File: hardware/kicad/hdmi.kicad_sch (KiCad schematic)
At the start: 1 part, among them J1 HDMI_C_1.4

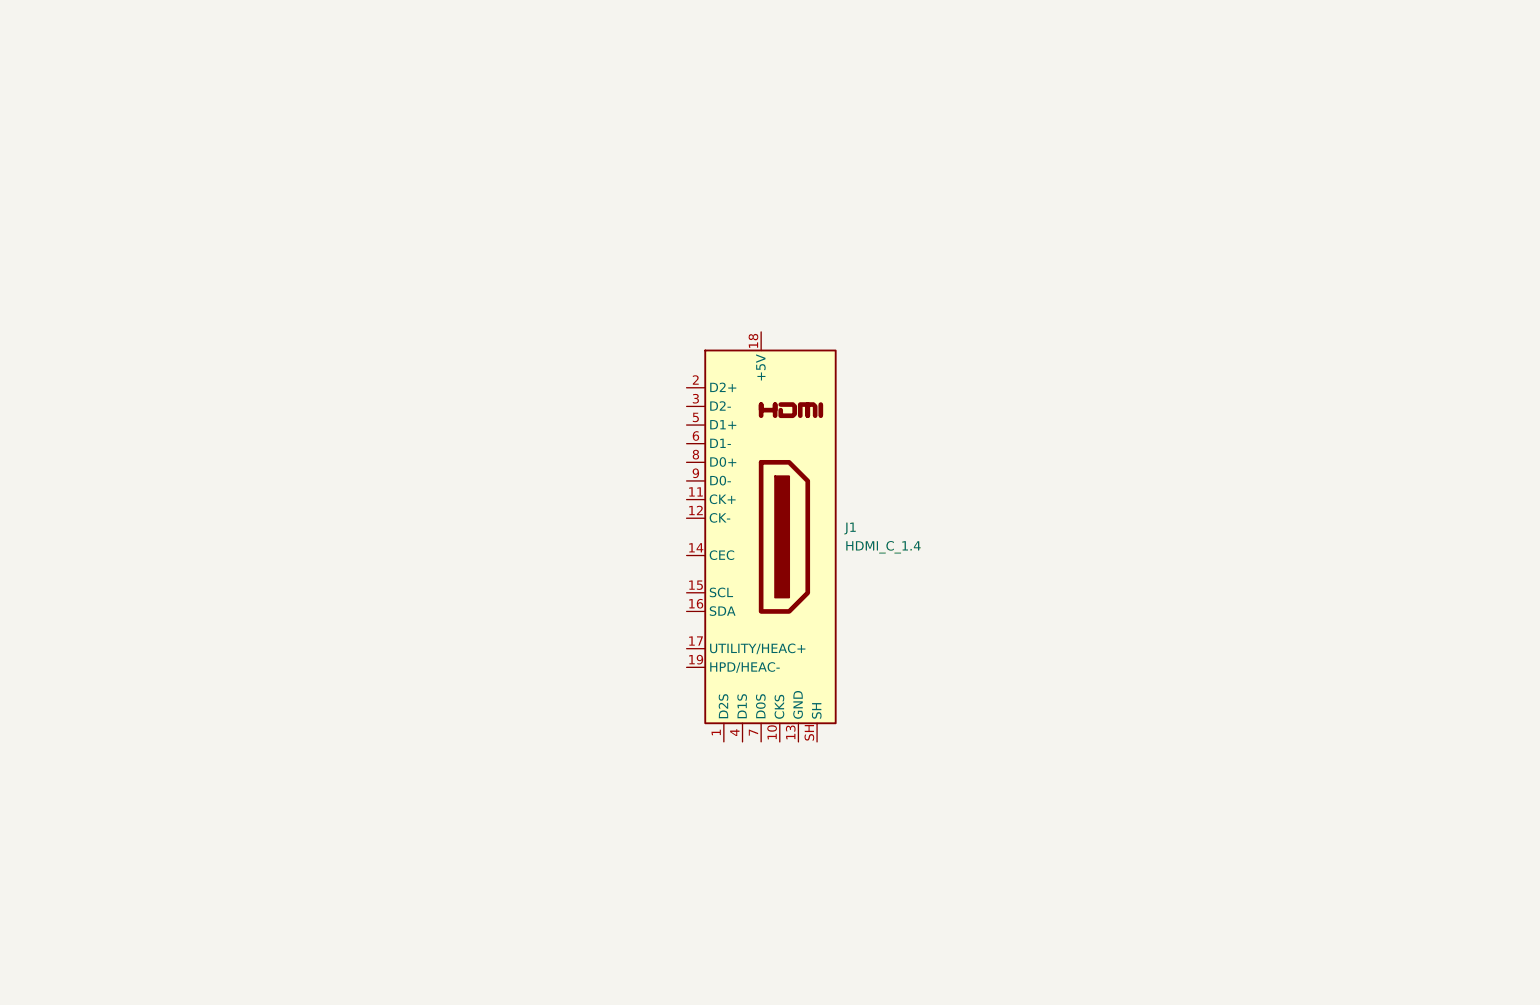
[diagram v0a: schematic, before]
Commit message: layout: finish dq0 & dq1 routing
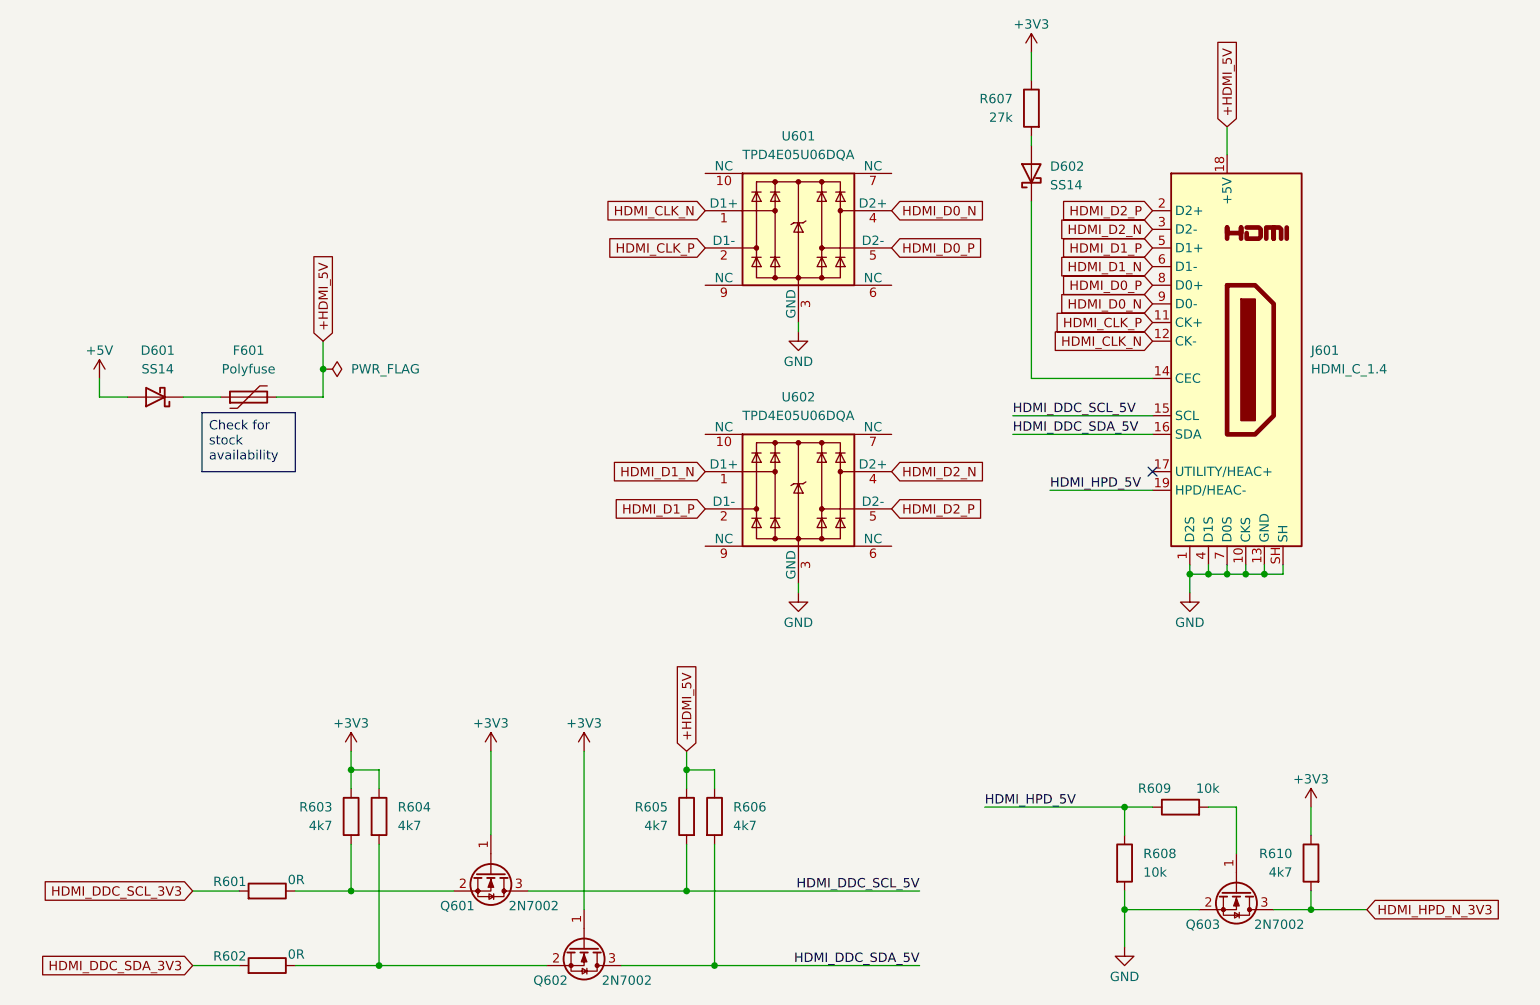
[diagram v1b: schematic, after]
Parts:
- added D601, D602: SS14, Diode_SMD:D_SMA, symbol Diode:SS14
- added F601: Polyfuse, Fuse:Fuse_0603_1608Metric, symbol Device:Polyfuse
- added Q601, Q602, Q603: 2N7002, Package_TO_SOT_SMD:SOT-23, symbol Transistor_FET:2N7002
- added R601, R602: 0R, Resistor_SMD:R_0402_1005Metric, symbol Device:R
- added R603, R604, R605, R606, R610: 4k7, Resistor_SMD:R_0402_1005Metric, symbol Device:R
- added R607: 27k, Resistor_SMD:R_0603_1608Metric, symbol Device:R
- added R608, R609: 10k, Resistor_SMD:R_0402_1005Metric, symbol Device:R
- added U601, U602: TPD4E05U06DQA, Package_SON:USON-10_2.5x1.0mm_P0.5mm, symbol Power_Protection:TPD4E05U06DQA
- renumbered J1 to J601
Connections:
- net GND: now reaches J601.1 (D2S)
- net GND: now also J601.10 (CKS), J601.13 (GND), J601.4 (D1S), J601.7 (D0S), J601.SH, Q603.2 (S), R608.2, U601.3 (GND), U601.8 (GND), U602.3 (GND), U602.8 (GND)
- net HDMI_CLK_P: now reaches J601.11 (CK+)
- net HDMI_CLK_P: now also U601.2 (D1-)
- net HDMI_CLK_N: now reaches J601.12 (CK-)
- net HDMI_CLK_N: now also U601.1 (D1+)
- net at J601.14 (CEC): now also D602.1 (K)
- net HDMI_DDC_SCL_5V: now reaches J601.15 (SCL)
- net HDMI_DDC_SCL_5V: now also Q601.3 (D), R605.2
- net HDMI_DDC_SDA_5V: now reaches J601.16 (SDA)
- net HDMI_DDC_SDA_5V: now also Q602.3 (D), R606.2
- net +HDMI_5V: now reaches J601.18 (+5V)
- net +HDMI_5V: now also F601.2, R605.1, R606.1
- net HDMI_HPD_5V: now reaches J601.19 (HPD/HEAC-)
- net HDMI_HPD_5V: now also R608.1, R609.1
- net HDMI_D2_P: now reaches J601.2 (D2+)
- net HDMI_D2_P: now also U602.5 (D2-)
- net HDMI_D2_N: now reaches J601.3 (D2-)
- net HDMI_D2_N: now also U602.4 (D2+)
- net HDMI_D1_P: now reaches J601.5 (D1+)
- net HDMI_D1_P: now also U602.2 (D1-)
- net HDMI_D1_N: now reaches J601.6 (D1-)
- net HDMI_D1_N: now also U602.1 (D1+)
- net HDMI_D0_P: now reaches J601.8 (D0+)
- net HDMI_D0_P: now also U601.5 (D2-)
- net HDMI_D0_N: now reaches J601.9 (D0-)
- net HDMI_D0_N: now also U601.4 (D2+)
- new net: Q603.1 (G), R609.2
- new net: D601.1 (K), F601.1
- new net: Q602.2 (S), R602.1, R604.2
- new net: D602.2 (A), R607.2
- new net: Q601.2 (S), R601.1, R603.2
- new net +3V3: Q601.1 (G), Q602.1 (G), R603.1, R604.1, R607.1, R610.1
- new net +5V: D601.2 (A)
- new net HDMI_DDC_SCL_3V3: R601.2
- new net HDMI_DDC_SDA_3V3: R602.2
- new net HDMI_HPD_N_3V3: Q603.3 (D), R610.2
- no-connect marks 0 -> 1
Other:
- moved on the sheet: J601

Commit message: finish basic ddr routing
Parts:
- removed J601: HDMI_C_1.4, Projects:HDMI-SMD_A71-05H4-111N1, symbol Connector:HDMI_C_1.4
- added J602: HDMI_A_1.4, Connector_Video:HDMI_A_Amphenol_10029449-x01xLF_Horizontal, symbol Connector:HDMI_A_1.4
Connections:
- net +HDMI_5V: now also J602.18 (+5V)
- net GND: now also J602.11 (CKS), J602.17 (GND), J602.2 (D2S), J602.5 (D1S), J602.8 (D0S), J602.SH
- net HDMI_CLK_N: now also J602.12 (CK-)
- net HDMI_CLK_P: now also J602.10 (CK+)
- net HDMI_D0_N: now also J602.9 (D0-)
- net HDMI_D0_P: now also J602.7 (D0+)
- net HDMI_D1_N: now also J602.6 (D1-)
- net HDMI_D1_P: now also J602.4 (D1+)
- net HDMI_D2_N: now also J602.3 (D2-)
- net HDMI_D2_P: now also J602.1 (D2+)
- net HDMI_DDC_SCL_5V: now also J602.15 (SCL)
- net HDMI_DDC_SDA_5V: now also J602.16 (SDA)
- net HDMI_HPD_5V: now also J602.19 (HPD/HEAC-)
- net at D602.1 (K): now also J602.13 (CEC)
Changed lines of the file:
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@@
+	)
+	(symbol
+		(lib_id "Connector:HDMI_A_1.4")
+		(at 207.01 63.5 0)
+		(unit 1)
+		(body_style 1)
+		(exclude_from_sim no)
+		(in_bom yes)
+		(on_board yes)
+		(in_pos_files yes)
+		(dnp no)
+		(fields_autoplaced yes)
+		(property "Reference" "J602"
+			(at 218.44 62.2299 0)
+			(show_name no)
+			(do_not_autoplace no)
+			(effects
+				(font
+					(size 1.27 1.27)
+				)
+				(justify left)
+			)
+		)
+		(property "Value" "HDMI_A_1.4"
+			(at 218.44 64.7699 0)
+			(show_name no)
+			(do_not_autoplace no)
+			(effects
+				(font
+					(size 1.27 1.27)
+				)
+				(justify left)
+			)
+		)
+		(property "Footprint" "Connector_Video:HDMI_A_Amphenol_10029449-x01xLF_Horizontal"
+			(at 207.645 63.5 0)
+			(hide yes)
+			(show_name no)
+			(do_not_autoplace no)
+			(effects
+				(font
+					(size 1.27 1.27)
+				)
+			)
+		)
+		(property "Datasheet" "https://en.wikipedia.org/wiki/HDMI"
+			(at 207.645 63.5 0)
+			(hide yes)
+			(show_name no)
+			(do_not_autoplace no)
+			(effects
+				(font
+					(size 1.27 1.27)
+				)
+			)
+		)
+		(property "Description" "HDMI 1.4+ type A connector"
+			(at 207.01 63.5 0)
+			(hide yes)
+			(show_name no)
+			(do_not_autoplace no)
+			(effects
+				(font
+					(size 1.27 1.27)
+				)
+			)
+		)
+		(pin "6"
+		)
+		(pin "5"
+		)
+		(pin "4"
+		)
+		(pin "3"
+		)
+		(pin "2"
+		)
+		(pin "1"
+		)
+		(pin "7"
+		)
+		(pin "19"
+		)
+		(pin "SH"
+		)
+		(pin "8"
+		)
+		(pin "9"
+		)
+		(pin "10"
+		)
+		(pin "11"
+		)
+		(pin "12"
+		)
+		(pin "13"
+		)
+		(pin "14"
+		)
+		(pin "15"
+		)
+		(pin "16"
+		)
+		(pin "17"
+		)
+		(pin "18"
+		)
+		(instances
+			(project "ZYNQ_PI_Zero"
+				(path "/e0cc3273-981b-466d-ad17-67861c989a34/194bd49b-39b9-439e-9b76-18223c8ed8de"
+					(reference "J602")
+					(unit 1)
+				)
+			)
+		)
 	)
 	(symbol
@@
 	)
 	(symbol
-		(lib_id "Connector:HDMI_C_1.4")
-		(at 207.01 63.5 0)
-		(unit 1)
-		(body_style 1)
-		(exclude_from_sim no)
-		(in_bom yes)
-		(on_board yes)
-		(in_pos_files yes)
-		(dnp no)
-		(fields_autoplaced yes)
-		(property "Reference" "J601"
-			(at 218.44 62.2299 0)
-			(show_name no)
-			(do_not_autoplace no)
-			(effects
-				(font
-					(size 1.27 1.27)
-				)
-				(justify left)
-			)
-		)
-		(property "Value" "HDMI_C_1.4"
-			(at 218.44 64.7699 0)
-			(show_name no)
-			(do_not_autoplace no)
-			(effects
-				(font
-					(size 1.27 1.27)
-				)
-				(justify left)
-			)
-		)
-		(property "Footprint" "Projects:HDMI-SMD_A71-05H4-111N1"
-			(at 207.645 63.5 0)
-			(hide yes)
-			(show_name no)
-			(do_not_autoplace no)
-			(effects
-				(font
-					(size 1.27 1.27)
-				)
-			)
-		)
-		(property "Datasheet" "http://pinoutguide.com/PortableDevices/mini_hdmi_pinout.shtml"
-			(at 207.645 63.5 0)
-			(hide yes)
-			(show_name no)
-			(do_not_autoplace no)
-			(effects
-				(font
-					(size 1.27 1.27)
-				)
-			)
-		)
-		(property "Description" "HDMI 1.4+ type C connector"
-			(at 207.01 63.5 0)
-			(hide yes)
-			(show_name no)
-			(do_not_autoplace no)
-			(effects
-				(font
-					(size 1.27 1.27)
-				)
-			)
-		)
-		(pin "6"
-		)
-		(pin "5"
-		)
-		(pin "1"
-		)
-		(pin "2"
-		)
-		(pin "3"
-		)
-		(pin "4"
-		)
-		(pin "11"
-		)
-		(pin "14"
-		)
-		(pin "10"
-		)
-		(pin "7"
-		)
-		(pin "SH"
-		)
-		(pin "18"
-		)
-		(pin "17"
-		)
-		(pin "19"
-		)
-		(pin "15"
-		)
-		(pin "16"
-		)
-		(pin "8"
-		)
-		(pin "12"
-		)
-		(pin "9"
-		)
-		(pin "13"
-		)
-		(instances
-			(project "hdmi"
-				(path "/73962548-2d49-4c88-a3cb-78a30267d693"
-					(reference "J1")
-					(unit 1)
-				)
-			)
-			(project "ZYNQ_PI_Zero"
-				(path "/e0cc3273-981b-466d-ad17-67861c989a34/194bd49b-39b9-439e-9b76-18223c8ed8de"
-					(reference "J601")
-					(unit 1)
-				)
-			)
-		)
-	)
-	(symbol
 		(lib_id "Power_Protection:TPD4E05U06DQA")
 		(at 148.59 45.72 0)
@@
 		)
 	)
+	(group ""
+		(members "15ec8058-eab1-47b0-89ef-e2197ceaa15e" "393eb2c9-2556-4fee-b569-2b447a7b0a4b"
+			"53660a61-2632-4e15-adf6-5c5c47ac1d81" "a32247c4-e007-4166-9461-d745543ec6ca"
+			"c5efe4c3-ab68-4d84-91f1-3170fa4f51b5" "c7352788-c409-47d4-88d6-23826d82852c"
+			"c9fb8644-763e-4d68-aa22-a40db3cfe74b" "cbd01b89-5dcc-49a2-98e9-251aa4bc034f"
+		)
+	)

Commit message: feat: need switch two singals of SD inferface
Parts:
- F601: footprint Fuse:Fuse_0603_1608Metric -> Fuse:Fuse_0805_2012Metric
- J602: footprint Connector_Video:HDMI_A_Amphenol_10029449-x01xLF_Horizontal -> Project:HDMI-SMD_HDMI-19PIN-043_C2858275
- R608, R609: footprint Resistor_SMD:R_0402_1005Metric -> Resistor_SMD:R_0603_1608Metric
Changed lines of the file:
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@@
 			)
 		)
-		(property "Footprint" "Resistor_SMD:R_0402_1005Metric"
+		(property "Footprint" "Resistor_SMD:R_0603_1608Metric"
 			(at 200.66 126.238 90)
 			(hide yes)
@@
 			)
 		)
-		(property "Footprint" "Connector_Video:HDMI_A_Amphenol_10029449-x01xLF_Horizontal"
+		(property "Footprint" "Project:HDMI-SMD_HDMI-19PIN-043_C2858275"
 			(at 207.645 63.5 0)
 			(hide yes)
@@
 			)
 		)
-		(property "Footprint" "Fuse:Fuse_0603_1608Metric"
+		(property "Footprint" "Fuse:Fuse_0805_2012Metric"
 			(at 78.74 67.31 0)
 			(hide yes)
@@
 			)
 		)
-		(property "Footprint" "Resistor_SMD:R_0402_1005Metric"
+		(property "Footprint" "Resistor_SMD:R_0603_1608Metric"
 			(at 191.262 132.08 90)
 			(hide yes)
